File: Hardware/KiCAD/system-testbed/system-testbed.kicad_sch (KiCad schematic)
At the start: 10 parts, among them J2 Stemma QT, J3 Stemma QT, J4 Stemma QT, X4 EYESPI, X5 EYESPI, X6 EYESPI

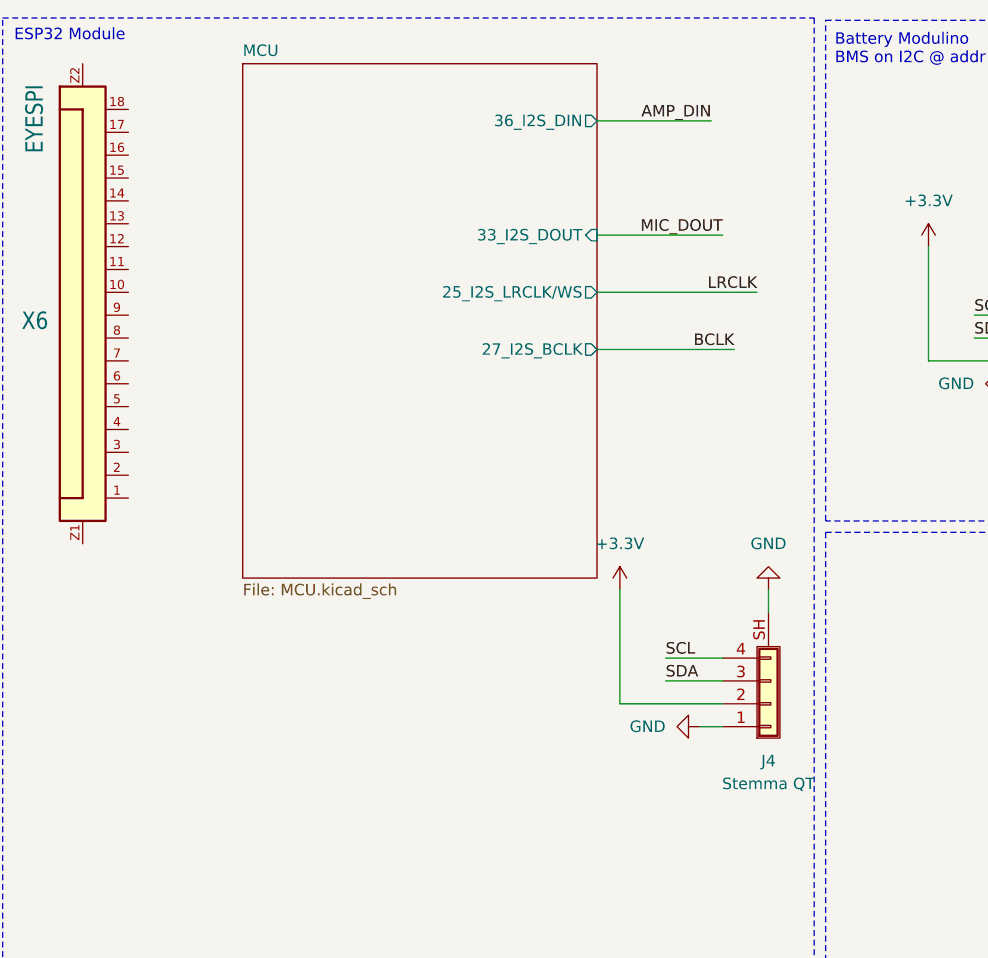
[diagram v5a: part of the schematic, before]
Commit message: feat: added WROVER footprint to project library & symbol
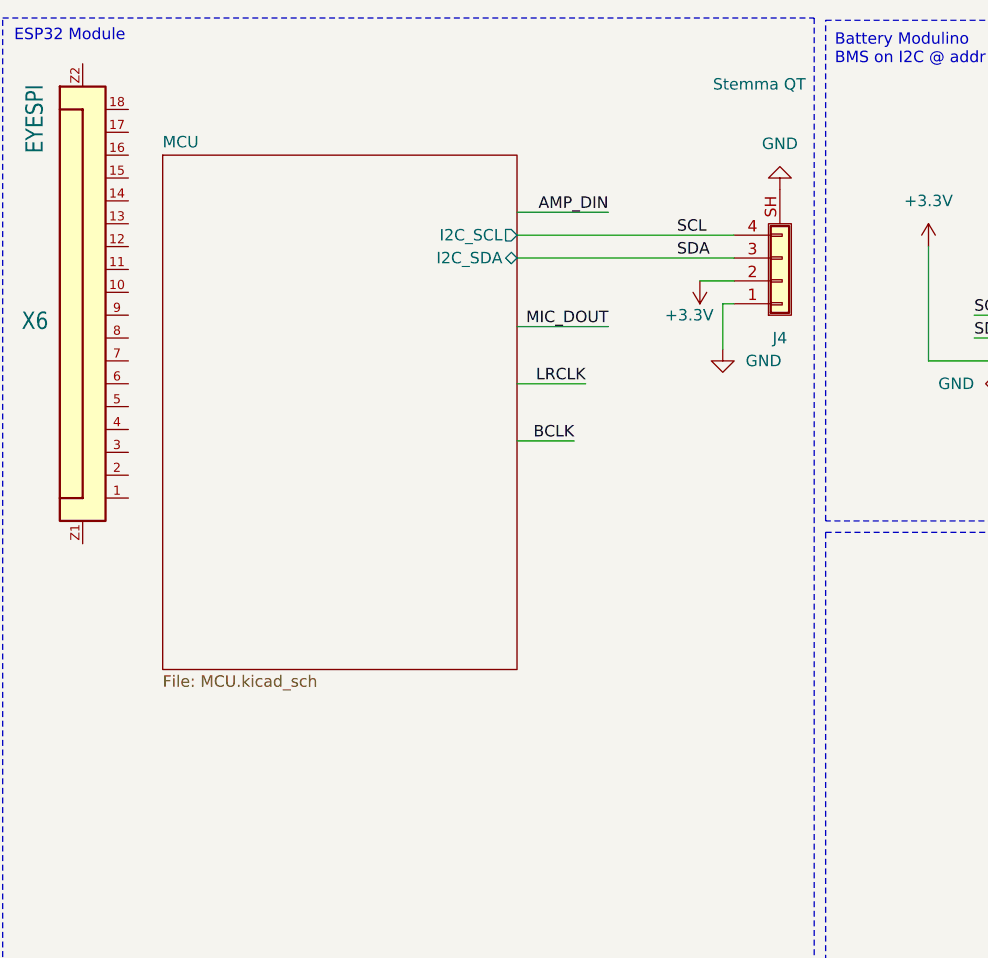
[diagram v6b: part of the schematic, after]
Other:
- sheet MCU ports: added I2C_SCL, I2C_SDA; removed 25_I2S_LRCLK/WS, 27_I2S_BCLK, 33_I2S_DOUT, 36_I2S_DIN
- moved on the sheet: J4
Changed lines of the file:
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@@
 	(wire
 		(pts
-			(xy 80.01 38.1) (xy 93.98 38.1)
+			(xy 71.12 48.26) (xy 81.28 48.26)
 		)
 		(stroke
@@
 	(wire
 		(pts
-			(xy 82.55 77.47) (xy 82.55 90.17)
-		)
-		(stroke
-			(width 0)
-			(type default)
-		)
-	)
-	(wire
-		(pts
-			(xy 99.06 77.47) (xy 99.06 80.01)
+			(xy 71.12 40.64) (xy 95.25 40.64)
 		)
 		(stroke
@@
 	(wire
 		(pts
-			(xy 80.01 44.45) (xy 97.79 44.45)
+			(xy 71.12 54.61) (xy 78.74 54.61)
+		)
+		(stroke
+			(width 0)
+			(type default)
+		)
+	)
+	(wire
+		(pts
+			(xy 93.98 45.72) (xy 93.98 50.8)
 		)
 		(stroke
@@
 	(wire
 		(pts
-			(xy 92.71 25.4) (xy 80.01 25.4)
+			(xy 81.28 35.56) (xy 71.12 35.56)
 		)
 		(stroke
@@
 	(wire
 		(pts
-			(xy 80.01 50.8) (xy 95.25 50.8)
+			(xy 71.12 60.96) (xy 77.47 60.96)
 		)
 		(stroke
@@
 	(wire
 		(pts
-			(xy 93.98 90.17) (xy 82.55 90.17)
+			(xy 95.25 43.18) (xy 91.44 43.18)
 		)
 		(stroke
@@
 	(wire
 		(pts
-			(xy 91.44 92.71) (xy 93.98 92.71)
-		)
-		(stroke
-			(width 0)
-			(type default)
-		)
-	)
-	(wire
-		(pts
-			(xy 93.98 85.09) (xy 87.63 85.09)
+			(xy 93.98 45.72) (xy 95.25 45.72)
 		)
 		(stroke
@@
 	(wire
 		(pts
-			(xy 93.98 87.63) (xy 87.63 87.63)
+			(xy 71.12 38.1) (xy 95.25 38.1)
 		)
 		(stroke
@@
 	)
 	(label "LRCLK"
-		(at 97.79 44.45 180)
+		(at 78.74 54.61 180)
 		(effects
 			(font
@@
 	)
 	(label "AMP_DIN"
-		(at 92.71 25.4 180)
+		(at 81.28 35.56 180)
 		(effects
 			(font
@@
 	)
 	(label "MIC_DOUT"
-		(at 93.98 38.1 180)
+		(at 81.28 48.26 180)
 		(effects
 			(font
@@
 	)
 	(label "SCL"
-		(at 87.63 85.09 0)
+		(at 88.9 38.1 0)
 		(effects
 			(font
@@
 	)
 	(label "SDA"
-		(at 87.63 87.63 0)
+		(at 88.9 40.64 0)
 		(effects
 			(font
@@
 	)
 	(label "BCLK"
-		(at 95.25 50.8 180)
+		(at 77.47 60.96 180)
 		(effects
 			(font
@@
 	(symbol
 		(lib_id "power:GND")
-		(at 99.06 77.47 0)
+		(at 100.33 33.02 0)
 		(mirror x)
 		(unit 1)
@@
 		(fields_autoplaced yes)
 		(property "Reference" "#PWR0170"
-			(at 99.06 71.12 0)
+			(at 100.33 26.67 0)
 			(effects
 				(font
@@
 		)
 		(property "Value" "GND"
-			(at 99.06 72.39 0)
+			(at 100.33 27.94 0)
 			(effects
 				(font
@@
 		)
 		(property "Footprint" ""
-			(at 99.06 77.47 0)
+			(at 100.33 33.02 0)
 			(effects
 				(font
@@
 		)
 		(property "Datasheet" ""
-			(at 99.06 77.47 0)
+			(at 100.33 33.02 0)
 			(effects
 				(font
@@
 		)
 		(property "Description" "Power symbol creates a global label with name \"GND\" , ground"
-			(at 99.06 77.47 0)
+			(at 100.33 33.02 0)
 			(effects
 				(font
@@
 		(dnp no)
 		(fields_autoplaced yes)
-		(property "Reference" "#PWR0136"
+		(property "Reference" "#PWR0172"
 			(at 17.78 194.31 0)
 			(effects
@@
 			(project "system-testbed"
 				(path "/72756aea-0ff9-4757-9699-8d0f18588f6f"
-					(reference "#PWR0136")
+					(reference "#PWR0172")
 					(unit 1)
 				)
@@
 	(symbol
 		(lib_id "power:+3.3V")
-		(at 82.55 77.47 0)
-		(mirror y)
+		(at 91.44 43.18 0)
+		(mirror x)
 		(unit 1)
 		(exclude_from_sim no)
@@
 		(on_board yes)
 		(dnp no)
-		(fields_autoplaced yes)
 		(property "Reference" "#PWR0168"
-			(at 82.55 81.28 0)
+			(at 91.44 39.37 0)
 			(effects
 				(font
@@
 		)
 		(property "Value" "+3.3V"
-			(at 82.55 72.39 0)
+			(at 92.964 46.99 0)
 			(effects
 				(font
 					(size 1.27 1.27)
 				)
+				(justify right)
 			)
 		)
 		(property "Footprint" ""
-			(at 82.55 77.47 0)
+			(at 91.44 43.18 0)
 			(effects
 				(font
@@
 		)
 		(property "Datasheet" ""
-			(at 82.55 77.47 0)
+			(at 91.44 43.18 0)
 			(effects
 				(font
@@
 		)
 		(property "Description" "Power symbol creates a global label with name \"+3.3V\""
-			(at 82.55 77.47 0)
+			(at 91.44 43.18 0)
 			(effects
 				(font
@@
 	(symbol
 		(lib_id "power:GND")
-		(at 91.44 92.71 270)
-		(mirror x)
+		(at 93.98 50.8 0)
+		(mirror y)
 		(unit 1)
 		(exclude_from_sim no)
@@
 		(fields_autoplaced yes)
 		(property "Reference" "#PWR0169"
-			(at 85.09 92.71 0)
+			(at 93.98 57.15 0)
 			(effects
 				(font
@@
 		)
 		(property "Value" "GND"
-			(at 87.63 92.7099 90)
+			(at 96.52 52.0699 0)
 			(effects
 				(font
@@
 		)
 		(property "Footprint" ""
-			(at 91.44 92.71 0)
+			(at 93.98 50.8 0)
 			(effects
 				(font
@@
 		)
 		(property "Datasheet" ""
-			(at 91.44 92.71 0)
+			(at 93.98 50.8 0)
 			(effects
 				(font
@@
 		)
 		(property "Description" "Power symbol creates a global label with name \"GND\" , ground"
-			(at 91.44 92.71 0)
+			(at 93.98 50.8 0)
 			(effects
 				(font
@@
 	(symbol
 		(lib_id "Connector_Generic_Shielded:Conn_01x04_Shielded")
-		(at 99.06 90.17 0)
+		(at 100.33 43.18 0)
 		(mirror x)
 		(unit 1)
@@
 		(on_board yes)
 		(dnp no)
-		(fields_autoplaced yes)
 		(property "Reference" "J4"
-			(at 99.06 96.52 0)
+			(at 100.33 49.53 0)
 			(effects
 				(font
@@
 		)
 		(property "Value" "Stemma QT"
-			(at 99.06 99.06 0)
+			(at 98.044 21.336 0)
 			(effects
 				(font
@@
 		)
 		(property "Footprint" "Connector_JST:JST_SH_SM04B-SRSS-TB_1x04-1MP_P1.00mm_Horizontal"
-			(at 99.06 90.17 0)
+			(at 100.33 43.18 0)
 			(effects
 				(font
@@
 		)
 		(property "Datasheet" "https://cdn-shop.adafruit.com/product-files/4208/4208_Kaweei_C13396_diagram.pdf"
-			(at 99.06 90.17 0)
+			(at 100.33 43.18 0)
 			(effects
 				(font
@@
 		)
 		(property "Description" "Generic shielded connector, single row, 01x04, script generated (kicad-library-utils/schlib/autogen/connector/)"
-			(at 99.06 90.17 0)
+			(at 100.33 43.18 0)
 			(effects
 				(font
@@
 	)
 	(sheet
-		(at 40.64 19.05)
+		(at 31.75 29.21)
 		(size 39.37 57.15)
 		(exclude_from_sim no)
@@
 		)
 		(property "Sheetname" "MCU"
-			(at 40.64 18.3384 0)
+			(at 31.75 28.4984 0)
 			(effects
 				(font
@@
 		)
 		(property "Sheetfile" "MCU.kicad_sch"
-			(at 40.64 76.7846 0)
+			(at 31.75 86.9446 0)
 			(effects
 				(font
@@
 			)
 		)
-		(pin "36_I2S_DIN" output
-			(at 80.01 25.4 0)
-			(effects
-				(font
-					(size 1.27 1.27)
-				)
-				(justify right)
-			)
-		)
-		(pin "33_I2S_DOUT" input
-			(at 80.01 38.1 0)
-			(effects
-				(font
-					(size 1.27 1.27)
-				)
-				(justify right)
-			)
-		)
-		(pin "25_I2S_LRCLK{slash}WS" output
-			(at 80.01 44.45 0)
+		(pin "I2C_SDA" bidirectional
+			(at 71.12 40.64 0)
 			(effects
 				(font
@@
 			)
 		)
-		(pin "27_I2S_BCLK" output
-			(at 80.01 50.8 0)
+		(pin "I2C_SCL" output
+			(at 71.12 38.1 0)
 			(effects
 				(font

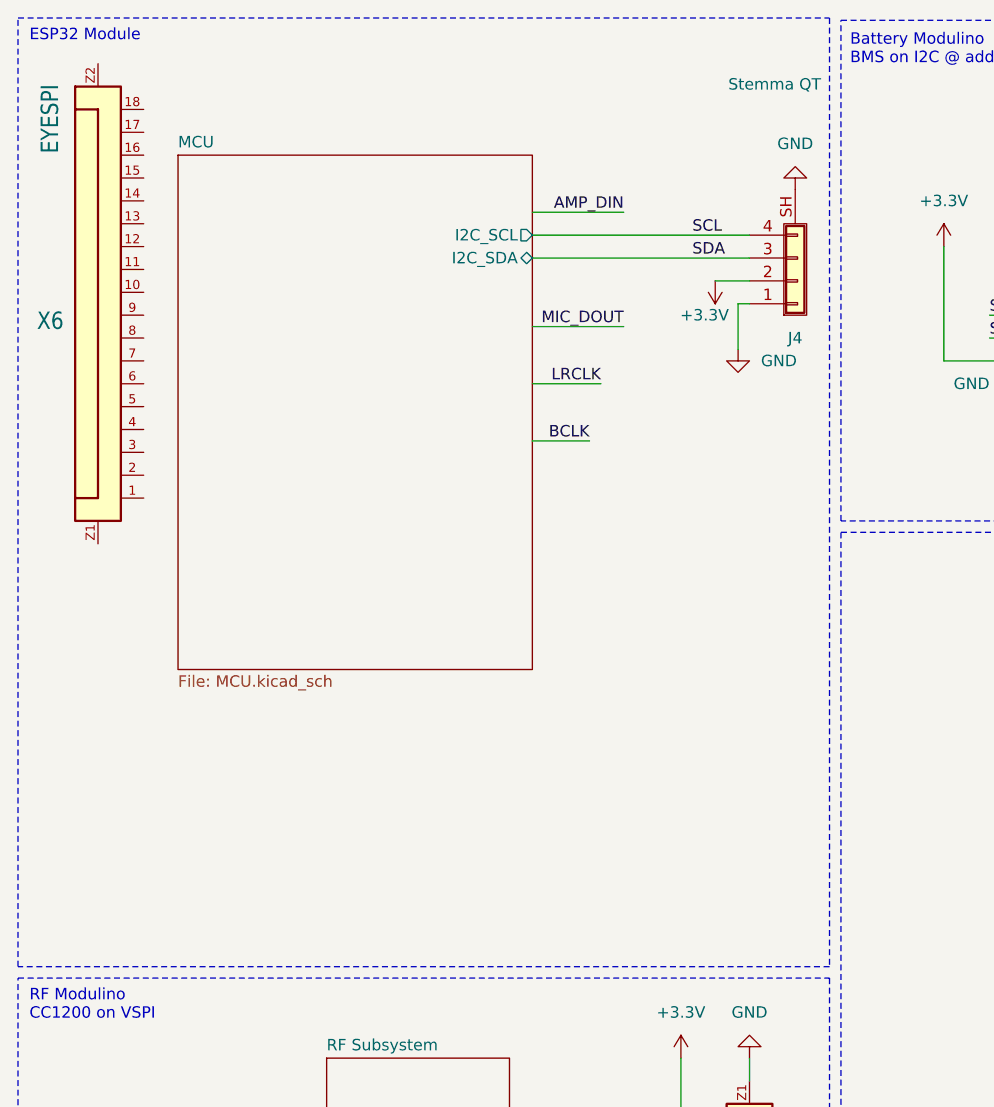
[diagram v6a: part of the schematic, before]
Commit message: feat: MCU changes to root labels & passive component sizes #63
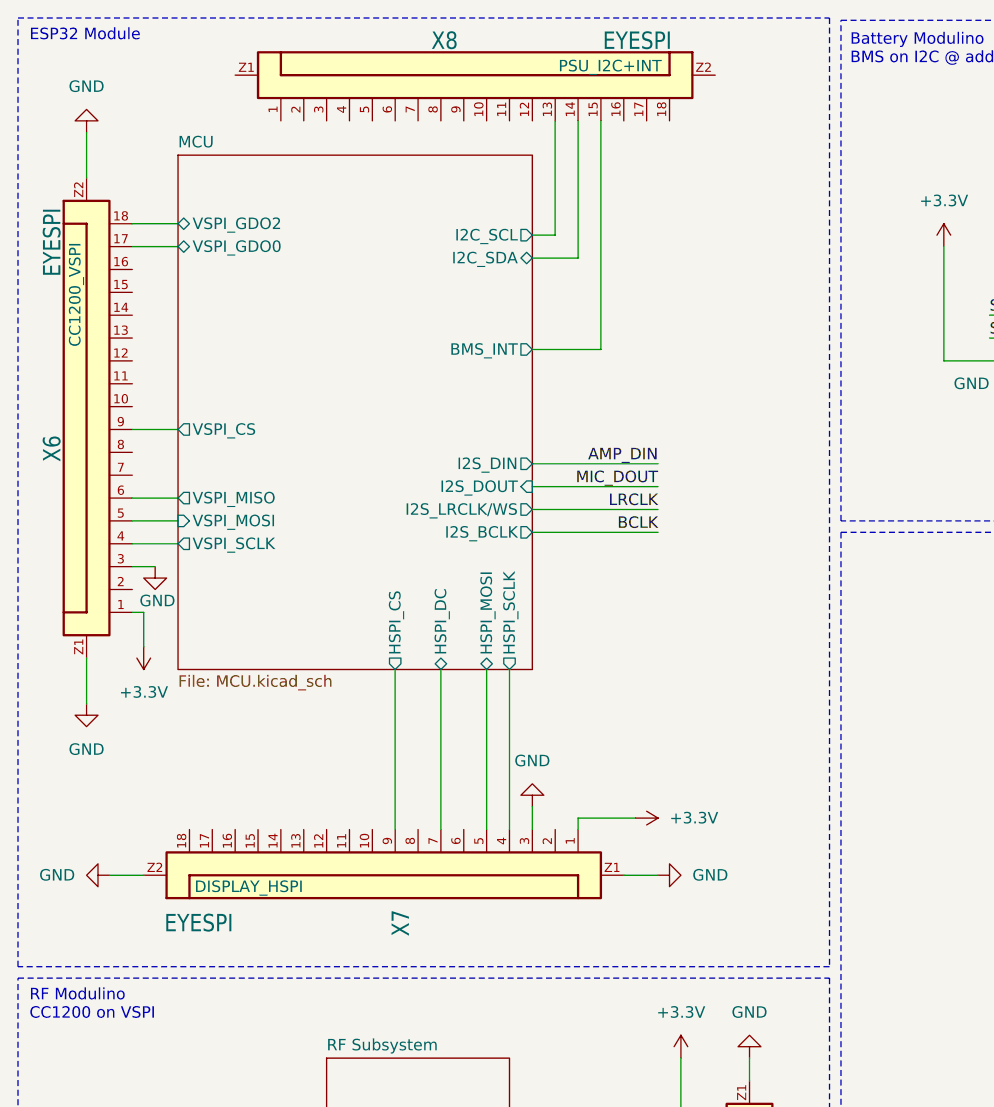
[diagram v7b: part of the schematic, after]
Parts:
- removed J4: Stemma QT, Connector_JST:JST_SH_SM04B-SRSS-TB_1x04-1MP_P1.00mm_Horizontal, symbol Connector_Generic_Shielded:Conn_01x04_Shielded
- added X7, X8: EYESPI, capstone-project:Adafruit EYESPI FPC Connector, symbol capstone-project:Adafruit EYESPI FPC Connector
- X6: Assignment (none) -> CC1200_VSPI
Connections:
- net +3.3V: now also X6.1, X7.1
- net GND: now also X6.3, X6.Z1, X6.Z2, X7.3, X7.Z1, X7.Z2
- net MCU/VSPI_GDO0: now reaches X6.17
- net MCU/VSPI_GDO2: now reaches X6.18
- net MCU/VSPI_SCLK: now reaches X6.4
- net MCU/VSPI_MOSI: now reaches X6.5
- net MCU/VSPI_MISO: now reaches X6.6
- net MCU/VSPI_CS: now reaches X6.9
- new net MCU/BMS_INT: X8.15
- new net MCU/HSPI_CS: X7.9
- new net MCU/HSPI_DC: X7.7
- new net MCU/HSPI_MOSI: X7.5
- new net MCU/HSPI_SCLK: X7.4
- new net MCU/I2C_SCL: X8.13
- new net MCU/I2C_SDA: X8.14
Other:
- sheet MCU ports: added BMS_INT, HSPI_CS, HSPI_DC, HSPI_MOSI, HSPI_SCLK, I2S_BCLK, I2S_DIN, I2S_DOUT, I2S_LRCLK/WS, VSPI_CS, VSPI_GDO0, VSPI_GDO2, VSPI_MISO, VSPI_MOSI, VSPI_SCLK; removed none
- moved on the sheet: X6
